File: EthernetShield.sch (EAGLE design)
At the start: 75 parts, among them IC1 W5100SQFP80, IC2 MCP24AA025E48, Q1 2N7002, SW1 RESET

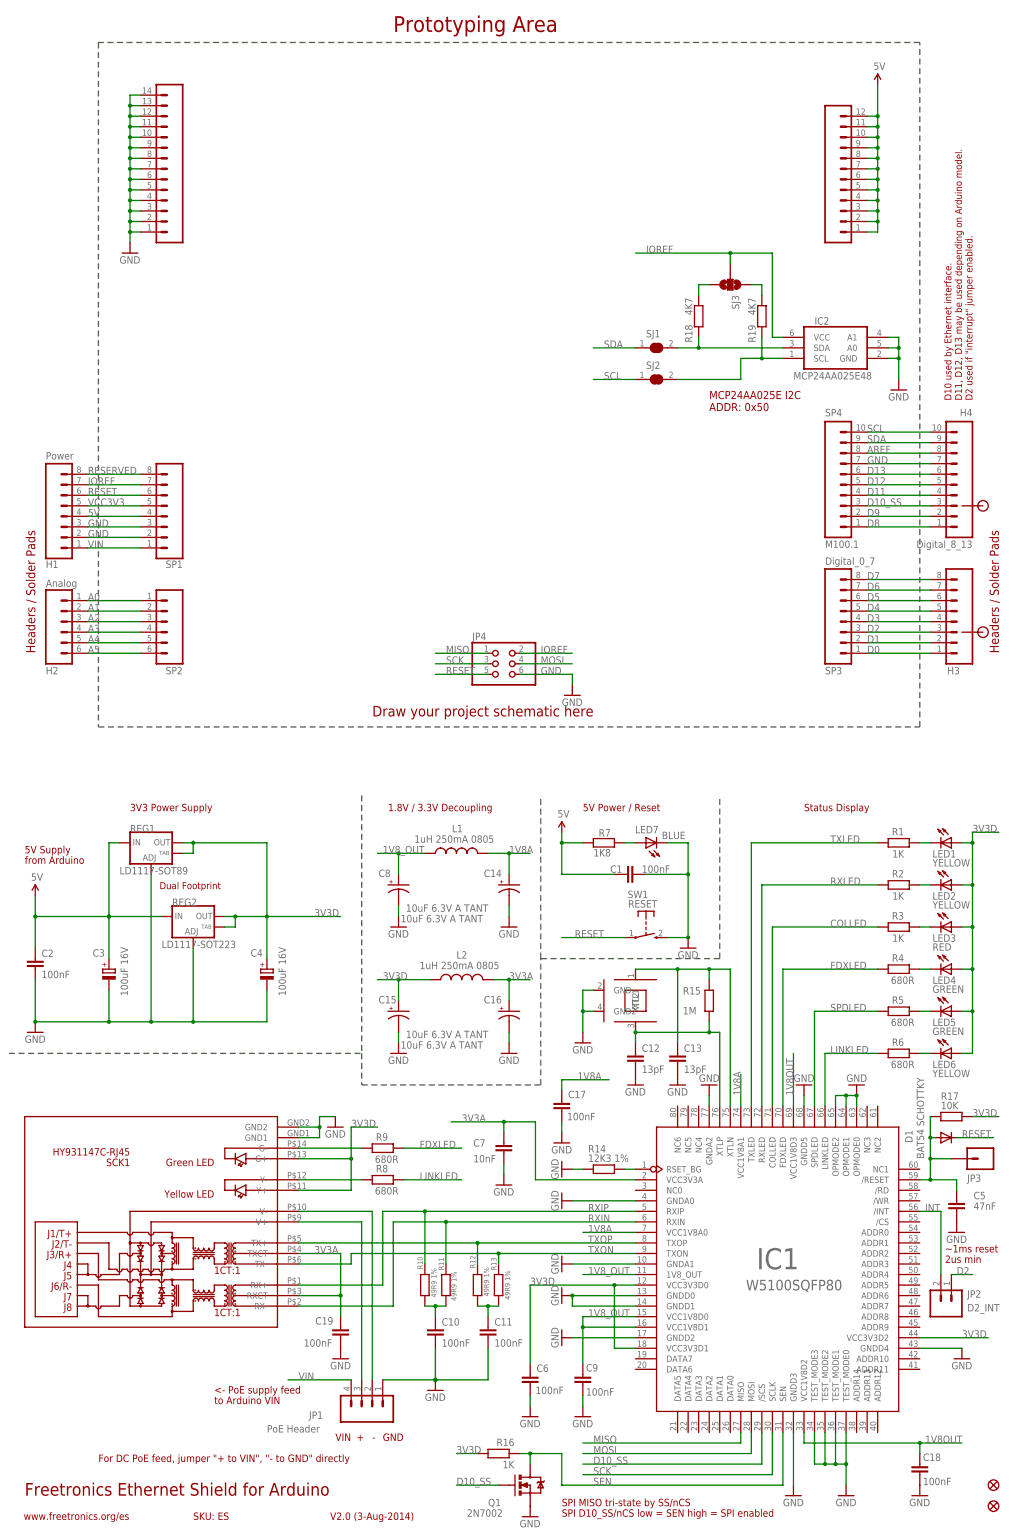
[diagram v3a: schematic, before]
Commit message: Began replacing W5100 with W5500
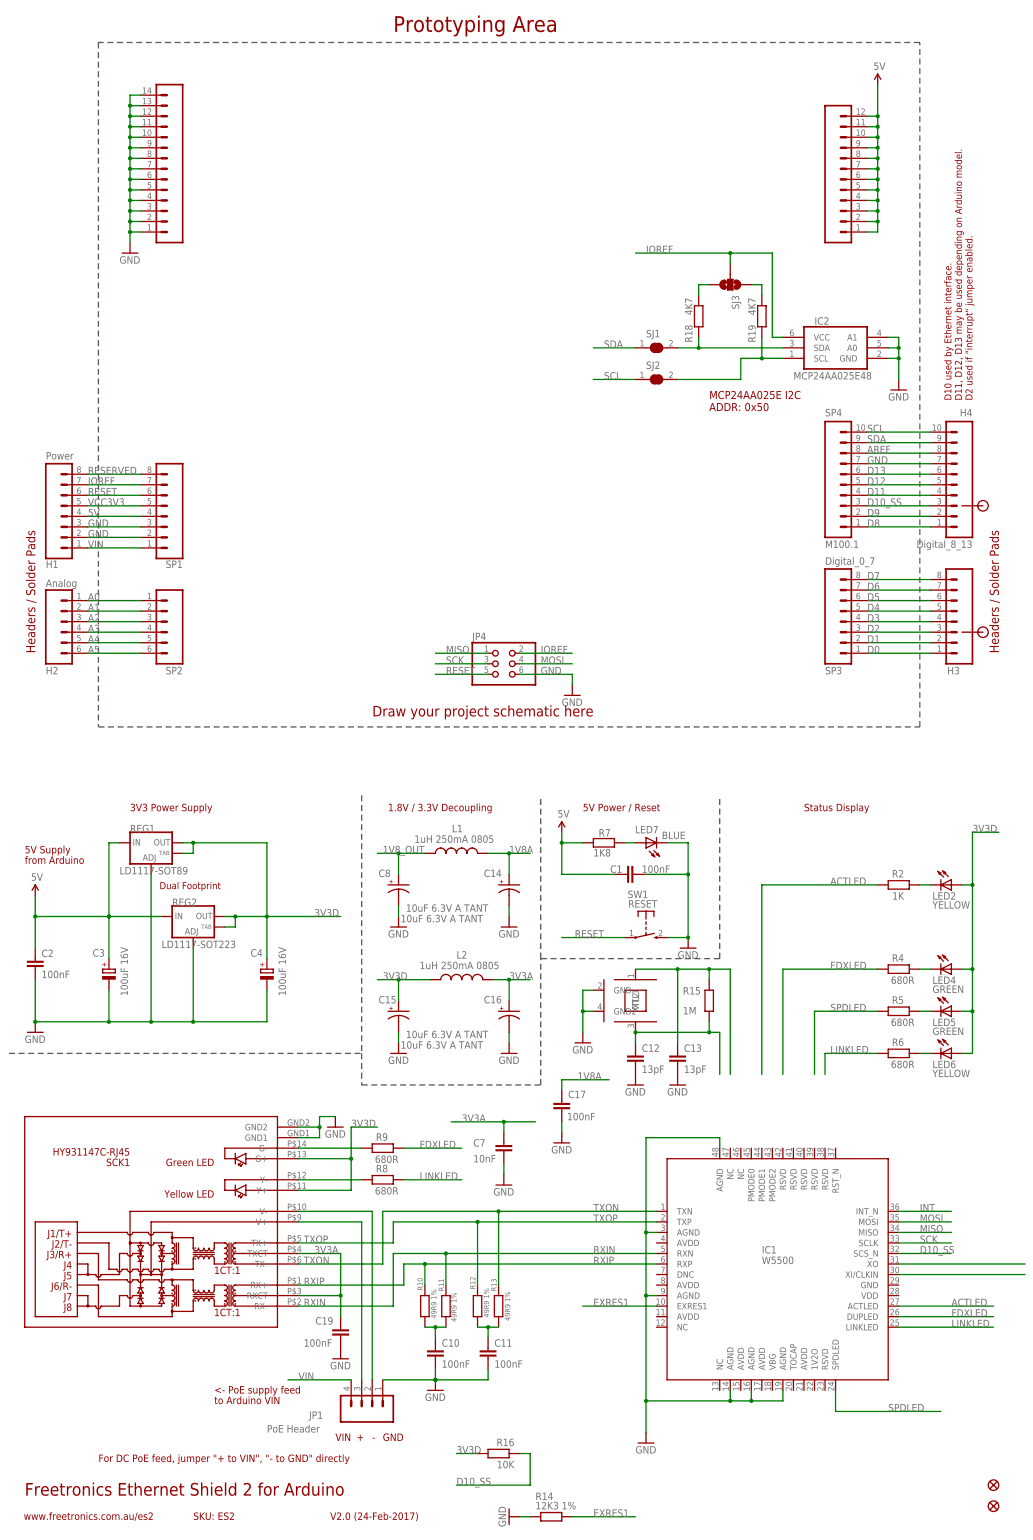
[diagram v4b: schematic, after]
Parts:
- removed C18, C6, C9: 100nF, freetronics:CAP0603
- removed C5: 47nF, freetronics:CAP0603
- removed D1: BAT54 SCHOTTKY, freetronics:DIODESOT23
- removed JP2: D2_INT, freetronics:M02PTH
- removed JP3: M01PTH, freetronics:M01PTH
- removed LED1: YELLOW, freetronics:LED0603
- removed LED3: RED, freetronics:LED0603
- removed Q1: 2N7002, freetronics:MOSFET-NCHANNELSMD
- removed R1, R3: 1K, freetronics:RESISTOR0603
- removed R17: 10K, freetronics:RESISTOR0603
- IC1: value W5100SQFP80 -> W5500; device freetronics-marc:W5100SQFP80 -> W5500:W5500
- R16: value 1K -> 10K
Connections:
- removed net 1V8OUT: C18.1, IC1.VCC1V8D2, IC1.VCC1V8D3
- removed net COLLED: IC1.COLLED, R3.2
- removed net N$322: IC1.RSET_BG, R14.2
- removed net N$328: LED3.C, R3.1
- removed net N$330: LED1.C, R1.1
- removed net N$70: C5.1, D1.A, IC1./RESET, JP3.1, R17.2
- removed net RXLED: IC1.RXLED, R2.2
- removed net SEN: IC1.SEN, Q1.D, R16.1
- removed net TXLED: IC1.TXLED, R1.2
- new net ACTLED: IC1.ACTLED, R2.2
- new net EXRES1: IC1.EXRES1, R14.2
- new net N$66: IC1.XO
- new net N$71: IC1.XI/CLKIN
- net 1V8A: no longer IC1.VCC1V8A0, IC1.VCC1V8A1
- net 1V8_OUT: no longer C9.1, IC1.1V8_OUT, IC1.VCC1V8D0, IC1.VCC1V8D1
- net 3V3A: no longer IC1.VCC3V3A
- net 3V3D: no longer C6.1, IC1.VCC3V3D0, IC1.VCC3V3D1, IC1.VCC3V3D2, LED1.A, LED3.A, R17.1
- net D10_SS: now also IC1.SCS_N, R16.1; no longer IC1./SCS, Q1.G
- net D2: no longer JP2.1
- net FDXLED: now also IC1.DUPLED; no longer IC1.FDXLED
- net GND: now also IC1.AGND@1, IC1.AGND@2, IC1.AGND@3, IC1.AGND@4, IC1.AGND@5, IC1.AGND@6; no longer C18.2, C5.2, C6.2, C9.2, IC1.GNDA0, IC1.GNDA1, IC1.GNDA2, IC1.GNDD0, IC1.GNDD1, IC1.GNDD2, IC1.GNDD3, IC1.GNDD4, IC1.GNDD5, IC1.OPMODE0, IC1.OPMODE1, IC1.OPMODE2, IC1.TEST_MODE0, IC1.TEST_MODE1, IC1.TEST_MODE2, IC1.TEST_MODE3, Q1.S
- net INT: now also IC1.INT_N; no longer IC1./INT, JP2.2
- net RESET: no longer D1.C
- net RXIN: now also IC1.RXN; no longer IC1.RXIN
- net RXIP: now also IC1.RXP; no longer IC1.RXIP
- net TXON: now also IC1.TXN; no longer IC1.TXON
- net TXOP: now also IC1.TXP; no longer IC1.TXOP
- net XTLN: no longer IC1.XTLN
- net XTLP: no longer IC1.XTLP
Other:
- note added: "Freetronics Ethernet Shield 2 for Arduino"
- note added: "SKU: ES2"
- note added: "V2.0 (24-Feb-2017)"
- note added: "www.freetronics.com.au/es2"
- note removed: "2us min"
- note removed: "Freetronics Ethernet Shield for Arduino"
- note removed: "SKU: ES"
- note removed: "SPI D10_SS/nCS low = SEN high = SPI enabled"
- note removed: "SPI MISO tri-state by SS/nCS"
- note removed: "V2.0 (3-Aug-2014)"
- note removed: "www.freetronics.org/es"
- note removed: "~1ms reset"
- moved on the sheet: C10, C11, R10, R11, R12, R13, R14
